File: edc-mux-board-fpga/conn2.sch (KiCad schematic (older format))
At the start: 24 parts

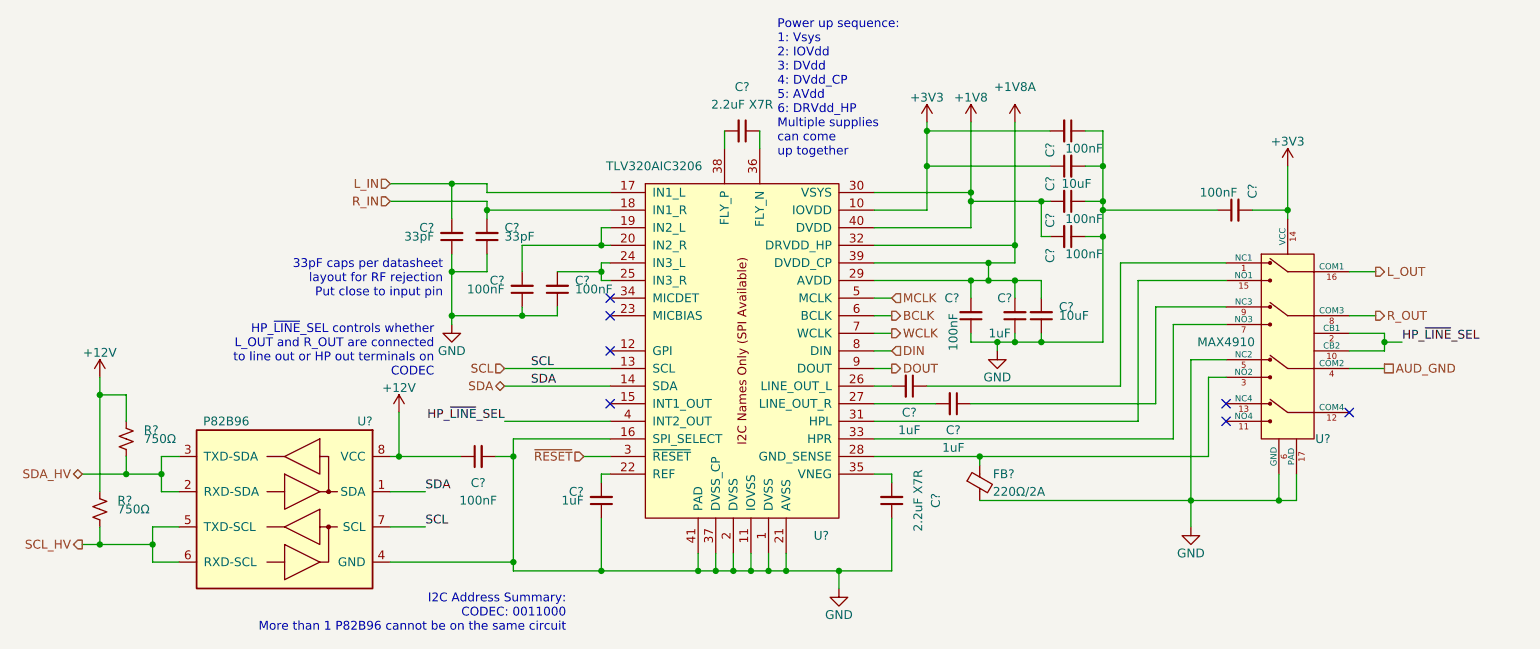
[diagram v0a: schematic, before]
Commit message: Finished FPGA and MCU interconnections.
Finished up interrupt wiring
Fixed a few missing connections
Annotated Schematic
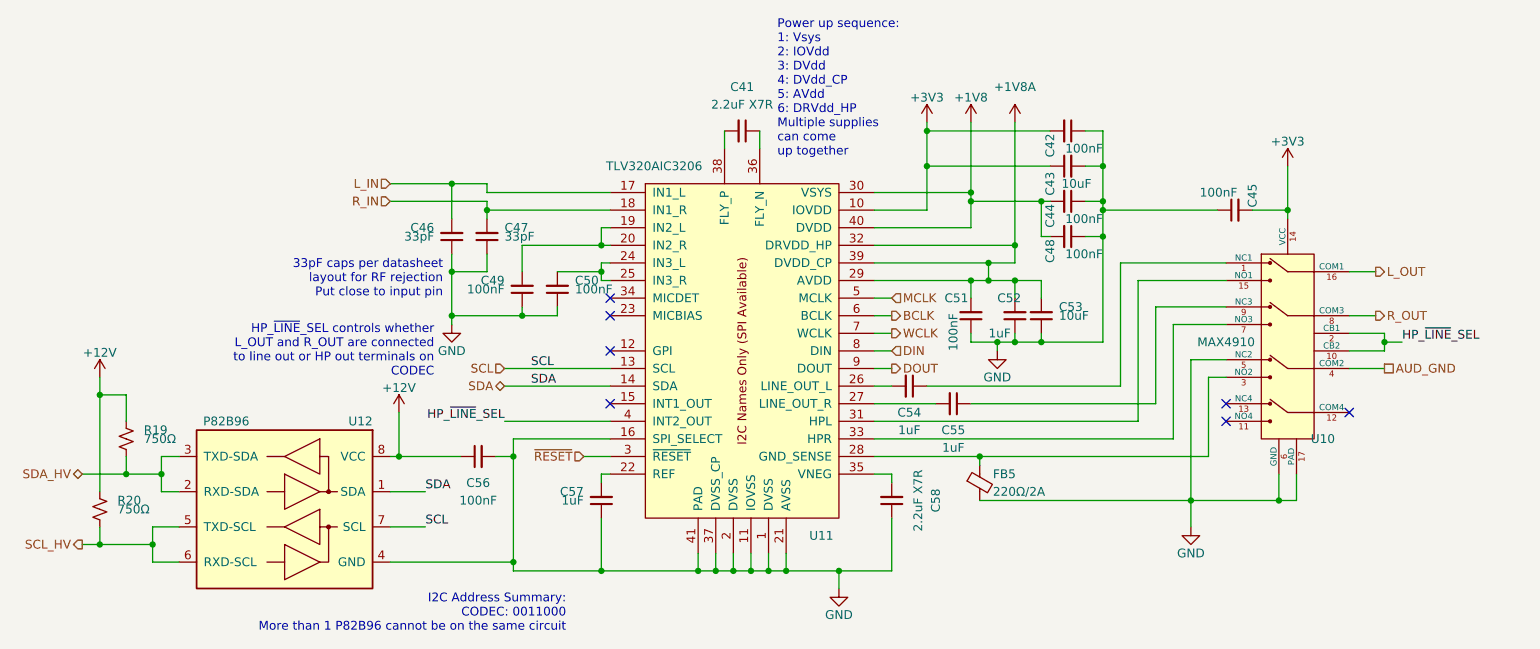
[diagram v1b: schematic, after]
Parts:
- removed C? (x2): 1uF, Capacitor_SMD:C_0805_2012Metric, symbol Device:C_Small
- removed C?: 2.2uF X7R, Capacitor_SMD:C_0603_1608Metric, symbol Device:C_Small
- removed C? (x2): 1uF, Capacitor_SMD:C_0603_1608Metric, symbol Device:C_Small
- removed C? (x8): 100nF, Capacitor_SMD:C_0603_1608Metric, symbol Device:C_Small
- removed C? (x2): 33pF, Capacitor_SMD:C_0603_1608Metric, symbol Device:C_Small
- removed C?: 10uF, Capacitor_SMD:C_1206_3216Metric, symbol Device:C_Small
- removed FB?: 220Ω/2A, Resistor_SMD:R_0603_1608Metric, symbol Device:Ferrite_Bead_Small
- removed R?: 750Ω, Resistor_SMD:R_0603_1608Metric, symbol Device:R_Small_US
- removed U?: TLV320AIC3206, Package_DFN_QFN:UQFN-40-1EP_5x5mm_P0.4mm_EP3.8x3.8mm_ThermalVias, symbol SW-Texas:TLV320AIC3206
- removed U?: MAX4910, Package_DFN_QFN:TQFN-16-1EP_3x3mm_P0.5mm_EP1.23x1.23mm, symbol SW-dallas-semi-maxim:MAX4910
- removed U?: P82B96, Package_SO:TSSOP-8_3x3mm_P0.65mm, symbol Interface_Expansion:P82B96
- added C42, C44, C45, C48, C49, C50, C51, C56: 100nF, Capacitor_SMD:C_0603_1608Metric, symbol Device:C_Small
- added C43: 10uF, Capacitor_SMD:C_1206_3216Metric, symbol Device:C_Small
- added C46, C47: 33pF, Capacitor_SMD:C_0603_1608Metric, symbol Device:C_Small
- added C52, C57: 1uF, Capacitor_SMD:C_0603_1608Metric, symbol Device:C_Small
- added C54, C55: 1uF, Capacitor_SMD:C_0805_2012Metric, symbol Device:C_Small
- added C58: 2.2uF X7R, Capacitor_SMD:C_0603_1608Metric, symbol Device:C_Small
- added FB5: 220Ω/2A, Resistor_SMD:R_0603_1608Metric, symbol Device:Ferrite_Bead_Small
- added R19: 750Ω, Resistor_SMD:R_0603_1608Metric, symbol Device:R_Small_US
- added U10: MAX4910, Package_DFN_QFN:TQFN-16-1EP_3x3mm_P0.5mm_EP1.23x1.23mm, symbol SW-dallas-semi-maxim:MAX4910
- added U11: TLV320AIC3206, Package_DFN_QFN:UQFN-40-1EP_5x5mm_P0.4mm_EP3.8x3.8mm_ThermalVias, symbol SW-Texas:TLV320AIC3206
- added U12: P82B96, Package_SO:TSSOP-8_3x3mm_P0.65mm, symbol Interface_Expansion:P82B96
- gave numbers to parts that had none: 3
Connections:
- net +12V: now also C56.1, R19.1, U12.8 (VCC)
- net +1V8: now also C44.2, C48.2, U11.30 (VSYS), U11.40 (DVDD)
- net +1V8A: now also C51.2, C52.2, U11.29 (AVDD), U11.32 (DRVDD_HP), U11.39 (DVDD_CP)
- net +3V3: now also C42.2, C43.1, C45.2, U10.14 (VCC), U11.10 (IOVDD)
- net AUD_GND: now also U10.4 (COM2)
- net BCLK: now also U11.6 (BCLK)
- net DIN: now also U11.8 (DIN)
- net DOUT: now also U11.9 (DOUT)
- net GND: now also C42.1, C43.2, C44.1, C45.1, C46.1, C47.1, C48.1, C49.1, C50.1, C51.1, C52.1, C56.2, C57.1, C58.1, FB5.2, U10.17 (PAD), U10.5 (NC2), U10.6 (GND), U11.1 (DVSS), U11.11 (IOVSS), U11.16 (SPI_SELECT), U11.2 (DVSS), U11.21 (AVSS), U11.37 (DVSS_CP), U11.41 (PAD), U12.4 (GND)
- net HP_~LINE~_SEL: now also U10.10 (CB2), U10.2 (CB1), U11.4 (INT2_OUT)
- net L_IN: now also C46.2, U11.17 (IN1_L)
- net L_OUT: now also U10.16 (COM1)
- net MCLK: now also U11.5 (MCLK)
- net R_IN: now also C47.2, U11.18 (IN1_R)
- net R_OUT: now also U10.8 (COM3)
- net SCL: now also U11.13 (SCL), U12.7 (SCL)
- net SCL_HV: now also U12.5 (TXD-SCL), U12.6 (RXD-SCL)
- net SDA: now also U11.14 (SDA), U12.1 (SDA)
- net SDA_HV: now also R19.2, U12.2 (RXD-SDA), U12.3 (TXD-SDA)
- net WCLK: now also U11.7 (WCLK)
- net ~RESET: now also U11.3 (~RESET)
- net at C41.1: now also U11.36 (FLY_N)
- net at C41.2: now also U11.38 (FLY_P)
- new net: C54.1, U10.1 (NC1)
- new net: C54.2, U11.26 (LINE_OUT_L)
- new net: C55.1, U10.9 (NC3)
- new net: C55.2, U11.27 (LINE_OUT_R)
- new net: C49.2, U11.19 (IN2_L), U11.20 (IN2_R)
- new net: C57.2, U11.22 (REF)
- new net: C50.2, U11.24 (IN3_L), U11.25 (IN3_R)
- new net: FB5.1, U10.3 (NO2), U11.28 (GND_SENSE)
- new net: U10.15 (NO1), U11.31 (HPL)
- new net: U10.7 (NO3), U11.33 (HPR)
- new net: C58.2, U11.35 (VNEG)
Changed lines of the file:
@@
 $EndDescr
 $Comp
-L SW-Texas:TLV320AIC3206 U?
-U 1 1 5CE6F2E7
+L SW-Texas:TLV320AIC3206 U11
+U 1 1 5DAC04B5
 P 5200 3400
-F 0 "U?" H 5650 2350 50  0000 C CNN
+F 0 "U11" H 5650 2350 50  0000 C CNN
 F 1 "TLV320AIC3206" H 4700 4450 50  0000 C CNN
 F 2 "Package_DFN_QFN:UQFN-40-1EP_5x5mm_P0.4mm_EP3.8x3.8mm_ThermalVias" H 5250 4800 50  0001 C CNN
@@
 $EndComp
 $Comp
-L Device:C_Small C?
+L Device:C_Small C41
 U 1 1 5CE6F309
 P 5200 2150
-F 0 "C?" V 4950 2150 50  0000 C CNN
+F 0 "C41" V 4950 2150 50  0000 C CNN
 F 1 "2.2uF X7R" V 5050 2150 50  0000 C CNN
 F 2 "Capacitor_SMD:C_0603_1608Metric" H 5200 2150 50  0001 C CNN
@@
 	5300 2250 5300 2150
 $Comp
-L Device:C_Small C?
-U 1 1 5CE6F311
+L Device:C_Small C58
+U 1 1 5DAC04CC
 P 6050 4250
-F 0 "C?" V 5800 4250 50  0000 C CNN
+F 0 "C58" V 5800 4250 50  0000 C CNN
 F 1 "2.2uF X7R" V 5900 4250 50  0000 C CNN
 F 2 "Capacitor_SMD:C_0603_1608Metric" H 6050 4250 50  0001 C CNN
@@
 	6050 4100 6050 4150
 $Comp
-L power:GND #PWR?
-U 1 1 5CE6F323
+L power:GND #PWR046
+U 1 1 5DAC04DB
 P 5750 4750
-F 0 "#PWR?" H 5750 4500 50  0001 C CNN
+F 0 "#PWR046" H 5750 4500 50  0001 C CNN
 F 1 "GND" H 5750 4600 50  0000 C CNN
 F 2 "" H 5750 4750 50  0001 C CNN
@@
 	5450 4650 5750 4650
 $Comp
-L Device:C_Small C?
-U 1 1 5CE6F329
+L Device:C_Small C57
+U 1 1 5DAC04F6
 P 4400 4250
-F 0 "C?" H 4500 4200 50  0000 L CNN
+F 0 "C57" H 4500 4200 50  0000 L CNN
 F 1 "1uF" H 4500 4250 50  0000 L CNN
 F 2 "Capacitor_SMD:C_0603_1608Metric" H 4400 4250 50  0001 C CNN
@@
 Connection ~ 4950 4650
 $Comp
-L Device:C_Small C?
-U 1 1 5CE6F348
+L Device:C_Small C49
+U 1 1 5DAC04FF
 P 3950 3050
-F 0 "C?" H 4050 3000 50  0000 L CNN
+F 0 "C49" H 4050 3000 50  0000 L CNN
 F 1 "100nF" H 4050 3050 50  0000 L CNN
 F 2 "Capacitor_SMD:C_0603_1608Metric" H 3950 3050 50  0001 C CNN
@@
 $EndComp
 $Comp
-L Device:C_Small C?
-U 1 1 5CE6F363
+L Device:C_Small C50
+U 1 1 5DAC050C
 P 4150 3050
-F 0 "C?" H 4050 3000 50  0000 R CNN
+F 0 "C50" H 4050 3000 50  0000 R CNN
 F 1 "100nF" H 4050 3050 50  0000 R CNN
 F 2 "Capacitor_SMD:C_0603_1608Metric" H 4150 3050 50  0001 C CNN
@@
 Connection ~ 4400 2950
 $Comp
-L power:GND #PWR?
-U 1 1 5CE6F368
+L power:GND #PWR041
+U 1 1 5DAC051C
 P 3550 3250
-F 0 "#PWR?" H 3550 3000 50  0001 C CNN
+F 0 "#PWR041" H 3550 3000 50  0001 C CNN
 F 1 "GND" H 3550 3100 50  0000 C CNN
 F 2 "" H 3550 3250 50  0001 C CNN
@@
 	8650 3300 8850 3300
 $Comp
-L SW-dallas-semi-maxim:MAX4910 U?
-U 1 1 5CE6F375
+L SW-dallas-semi-maxim:MAX4910 U10
+U 1 1 5DAC0526
 P 8300 3350
-F 0 "U?" H 8500 2800 50  0000 C CNN
+F 0 "U10" H 8500 2800 50  0000 C CNN
 F 1 "MAX4910" H 7950 3350 50  0000 C CNN
 F 2 "Package_DFN_QFN:TQFN-16-1EP_3x3mm_P0.5mm_EP1.23x1.23mm" H 9950 4500 50  0001 C CNN
@@
 	7750 3450 7750 4250
 $Comp
-L power:GND #PWR?
-U 1 1 5CE6F387
+L power:GND #PWR045
+U 1 1 5DAC0541
 P 7750 4400
-F 0 "#PWR?" H 7750 4150 50  0001 C CNN
+F 0 "#PWR045" H 7750 4150 50  0001 C CNN
 F 1 "GND" H 7750 4250 50  0000 C CNN
 F 2 "" H 7750 4400 50  0001 C CNN
@@
 	8650 3500 8850 3500
 $Comp
-L Device:Ferrite_Bead_Small FB?
-U 1 1 5CE6F39A
+L Device:Ferrite_Bead_Small FB5
+U 1 1 5DAC0551
 P 6550 4150
-F 0 "FB?" H 6625 4200 50  0000 L CNN
+F 0 "FB5" H 6625 4200 50  0000 L CNN
 F 1 "220Ω/2A" H 6625 4100 50  0000 L CNN
 F 2 "Resistor_SMD:R_0603_1608Metric" V 6480 4150 50  0001 C CNN
@@
 	3750 2600 4450 2600
 $Comp
-L Device:C_Small C?
-U 1 1 5CE6F3AC
+L Device:C_Small C46
+U 1 1 5DAC055E
 P 3550 2750
-F 0 "C?" H 3650 2700 50  0000 L CNN
+F 0 "C46" H 3650 2700 50  0000 L CNN
 F 1 "33pF" H 3650 2750 50  0000 L CNN
 F 2 "Capacitor_SMD:C_0603_1608Metric" H 3550 2750 50  0001 C CNN
@@
 	3200 2550 3750 2550
 $Comp
-L Device:C_Small C?
-U 1 1 5CE6F3B7
+L Device:C_Small C47
+U 1 1 5DAC056D
 P 3750 2750
-F 0 "C?" H 3650 2700 50  0000 R CNN
+F 0 "C47" H 3650 2700 50  0000 R CNN
 F 1 "33pF" H 3650 2750 50  0000 R CNN
 F 2 "Capacitor_SMD:C_0603_1608Metric" H 3750 2750 50  0001 C CNN
@@
 	5950 3000 6500 3000
 $Comp
-L SW-power:+1V8A #+1V8A?
-U 1 1 5CE6F3C8
+L SW-power:+1V8A #+1V8A04
+U 1 1 5DAC0576
 P 6750 2100
-F 0 "#+1V8A?" H 7500 1800 60  0001 C CNN
+F 0 "#+1V8A04" H 7500 1800 60  0001 C CNN
 F 1 "+1V8A" H 6750 2300 50  0000 C CNN
 F 2 "" H 6750 2100 60  0001 C CNN
@@
 $EndComp
 $Comp
-L power:+1V8 #PWR?
-U 1 1 5CE6F3D1
+L power:+1V8 #PWR039
+U 1 1 5DAC058D
 P 6500 2100
-F 0 "#PWR?" H 6500 1950 50  0001 C CNN
+F 0 "#PWR039" H 6500 1950 50  0001 C CNN
 F 1 "+1V8" H 6500 2240 50  0000 C CNN
 F 2 "" H 6500 2100 50  0001 C CNN
@@
 	6750 2800 6750 2900
 $Comp
-L power:+3V3 #PWR?
-U 1 1 5CE6F3E5
+L power:+3V3 #PWR038
+U 1 1 5DAC059C
 P 6250 2100
-F 0 "#PWR?" H 6250 1950 50  0001 C CNN
+F 0 "#PWR038" H 6250 1950 50  0001 C CNN
 F 1 "+3V3" H 6250 2240 50  0000 C CNN
 F 2 "" H 6250 2100 50  0001 C CNN
@@
 	6250 2600 6250 2350
 $Comp
-L Device:C_Small C?
-U 1 1 5CE6F3F4
+L Device:C_Small C52
+U 1 1 5DAC05A3
 P 6750 3200
-F 0 "C?" H 6850 3100 50  0000 R CNN
+F 0 "C52" H 6850 3100 50  0000 R CNN
 F 1 "1uF" H 6900 3300 50  0000 R CNN
 F 2 "Capacitor_SMD:C_0603_1608Metric" H 6750 3200 50  0001 C CNN
@@
 $EndComp
 $Comp
-L power:GND #PWR?
-U 1 1 5CE6F403
+L power:GND #PWR042
+U 1 1 5DAC05B5
 P 6650 3400
-F 0 "#PWR?" H 6650 3150 50  0001 C CNN
+F 0 "#PWR042" H 6650 3150 50  0001 C CNN
 F 1 "GND" H 6650 3250 50  0000 C CNN
 F 2 "" H 6650 3400 50  0001 C CNN
@@
 $EndComp
 $Comp
-L Device:C_Small C?
+L Device:C_Small C53
 U 1 1 5CE6F40F
 P 6900 3200
-F 0 "C?" H 6800 3150 50  0000 R CNN
+F 0 "C53" H 6800 3150 50  0000 R CNN
 F 1 "10uF" H 6800 3200 50  0000 R CNN
 F 2 "Capacitor_SMD:C_1206_3216Metric" H 6900 3200 50  0001 C CNN
@@
 $EndComp
 $Comp
-L Device:C_Small C?
-U 1 1 5CE6F425
+L Device:C_Small C51
+U 1 1 5DAC05CC
 P 6500 3200
-F 0 "C?" H 6650 3100 50  0000 R CNN
+F 0 "C51" H 6650 3100 50  0000 R CNN
 F 1 "100nF" V 6600 3400 50  0000 R CNN
 F 2 "Capacitor_SMD:C_0603_1608Metric" H 6500 3200 50  0001 C CNN
@@
 	6650 3350 6750 3350
 $Comp
-L Device:C_Small C?
-U 1 1 5CE6F42F
+L Device:C_Small C42
+U 1 1 5DAC05E4
 P 7050 2150
-F 0 "C?" H 7200 2050 50  0000 R CNN
+F 0 "C42" H 7200 2050 50  0000 R CNN
 F 1 "100nF" V 7150 2350 50  0000 R CNN
 F 2 "Capacitor_SMD:C_0603_1608Metric" H 7050 2150 50  0001 C CNN
@@
 $EndComp
 $Comp
-L Device:C_Small C?
-U 1 1 5CE6F439
+L Device:C_Small C43
+U 1 1 5DAC05EE
 P 7050 2350
-F 0 "C?" H 6950 2450 50  0000 C CNN
+F 0 "C43" H 6950 2450 50  0000 C CNN
 F 1 "10uF" V 6950 2300 50  0000 C CNN
 F 2 "Capacitor_SMD:C_1206_3216Metric" H 7050 2350 50  0001 C CNN
@@
 	6250 2150 6250 2100
 $Comp
-L Device:C_Small C?
-U 1 1 5CE6F451
+L Device:C_Small C44
+U 1 1 5DAC0601
 P 7050 2550
-F 0 "C?" H 7200 2450 50  0000 R CNN
+F 0 "C44" H 7200 2450 50  0000 R CNN
 F 1 "100nF" V 7150 2750 50  0000 R CNN
 F 2 "Capacitor_SMD:C_0603_1608Metric" H 7050 2550 50  0001 C CNN
@@
 	6500 2550 6500 2500
 $Comp
-L Device:C_Small C?
-U 1 1 5CE6F456
+L Device:C_Small C48
+U 1 1 5DAC0606
 P 7050 2750
-F 0 "C?" H 7200 2650 50  0000 R CNN
+F 0 "C48" H 7200 2650 50  0000 R CNN
 F 1 "100nF" V 7150 2950 50  0000 R CNN
 F 2 "Capacitor_SMD:C_0603_1608Metric" H 7050 2750 50  0001 C CNN
@@
 NoConn ~ 8650 3750
 $Comp
-L Device:C_Small C?
-U 1 1 5CE6F46F
+L Device:C_Small C45
+U 1 1 5DAC061C
 P 8000 2600
-F 0 "C?" H 8150 2500 50  0000 R CNN
+F 0 "C45" H 8150 2500 50  0000 R CNN
 F 1 "100nF" V 8100 2800 50  0000 R CNN
 F 2 "Capacitor_SMD:C_0603_1608Metric" H 8000 2600 50  0001 C CNN
@@
 $EndComp
 $Comp
-L power:+3V3 #PWR?
-U 1 1 5CE6F47E
+L power:+3V3 #PWR040
+U 1 1 5DAC0631
 P 8300 2350
-F 0 "#PWR?" H 8300 2200 50  0001 C CNN
+F 0 "#PWR040" H 8300 2200 50  0001 C CNN
 F 1 "+3V3" H 8300 2490 50  0000 C CNN
 F 2 "" H 8300 2350 50  0001 C CNN
@@
 	8250 4250 8350 4250
 $Comp
-L Interface_Expansion:P82B96 U?
-U 1 1 5CE6F489
+L Interface_Expansion:P82B96 U12
+U 1 1 5DAC0639
 P 2600 4300
-F 0 "U?" H 2100 4800 50  0000 L CNN
+F 0 "U12" H 2100 4800 50  0000 L CNN
 F 1 "P82B96" H 2800 4800 50  0000 L CNN
 F 2 "Package_SO:TSSOP-8_3x3mm_P0.65mm" H 2600 4300 50  0001 C CNN
@@
 $EndComp
 $Comp
-L power:+12V #PWR?
-U 1 1 5CE6F490
+L power:+12V #PWR043
+U 1 1 5DAC0650
 P 1550 3550
-F 0 "#PWR?" H 1550 3400 50  0001 C CNN
+F 0 "#PWR043" H 1550 3400 50  0001 C CNN
 F 1 "+12V" H 1550 3690 50  0000 C CNN
 F 2 "" H 1550 3550 50  0001 C CNN
@@
 	1900 4100 1900 4200
 $Comp
-L Device:R_Small_US R?
-U 1 1 5CE6F4C1
+L Device:R_Small_US R19
+U 1 1 5DAC0654
 P 1700 3900
-F 0 "R?" H 1800 3950 50  0000 L CNN
+F 0 "R19" H 1800 3950 50  0000 L CNN
 F 1 "750Ω" H 1800 3900 50  0000 L CNN
 F 2 "Resistor_SMD:R_0603_1608Metric" H 1700 3900 50  0001 C CNN
@@
 $EndComp
 $Comp
-L Device:R_Small_US R?
+L Device:R_Small_US R20
 U 1 1 5CE6F4D0
 P 1550 4300
-F 0 "R?" H 1650 4350 50  0000 L CNN
+F 0 "R20" H 1650 4350 50  0000 L CNN
 F 1 "750Ω" H 1650 4300 50  0000 L CNN
 F 2 "Resistor_SMD:R_0603_1608Metric" H 1550 4300 50  0001 C CNN
@@
 	1700 4100 1900 4100
 $Comp
-L power:+12V #PWR?
-U 1 1 5CE6F4E1
+L power:+12V #PWR044
+U 1 1 5DAC0678
 P 3250 3750
-F 0 "#PWR?" H 3250 3600 50  0001 C CNN
+F 0 "#PWR044" H 3250 3600 50  0001 C CNN
 F 1 "+12V" H 3250 3890 50  0000 C CNN
 F 2 "" H 3250 3750 50  0001 C CNN
@@
 	3200 4400 3400 4400
 $Comp
-L Device:C_Small C?
-U 1 1 5CE6F4F3
+L Device:C_Small C56
+U 1 1 5DAC0685
 P 3700 4000
-F 0 "C?" V 3550 4000 50  0000 C CNN
+F 0 "C56" V 3550 4000 50  0000 C CNN
 F 1 "100nF" V 3450 4000 50  0000 C CNN
 F 2 "Capacitor_SMD:C_0603_1608Metric" H 3700 4000 50  0001 C CNN
@@
 	1450 4500 1550 4500
 $Comp
-L Device:C_Small C?
-U 1 1 5CE6F2C0
+L Device:C_Small C54
+U 1 1 5DAC048F
 P 6150 3600
-F 0 "C?" V 6300 3600 50  0000 C CNN
+F 0 "C54" V 6300 3600 50  0000 C CNN
 F 1 "1uF" V 6400 3600 50  0000 C CNN
 F 2 "Capacitor_SMD:C_0805_2012Metric" H 6150 3600 50  0001 C CNN
@@
 $EndComp
 $Comp
-L Device:C_Small C?
-U 1 1 5CE6F2D4
+L Device:C_Small C55
+U 1 1 5DAC04A0
 P 6400 3700
-F 0 "C?" V 6550 3700 50  0000 C CNN
+F 0 "C55" V 6550 3700 50  0000 C CNN
 F 1 "1uF" V 6650 3700 50  0000 C CNN
 F 2 "Capacitor_SMD:C_0805_2012Metric" H 6400 3700 50  0001 C CNN

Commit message: assigned more footprints
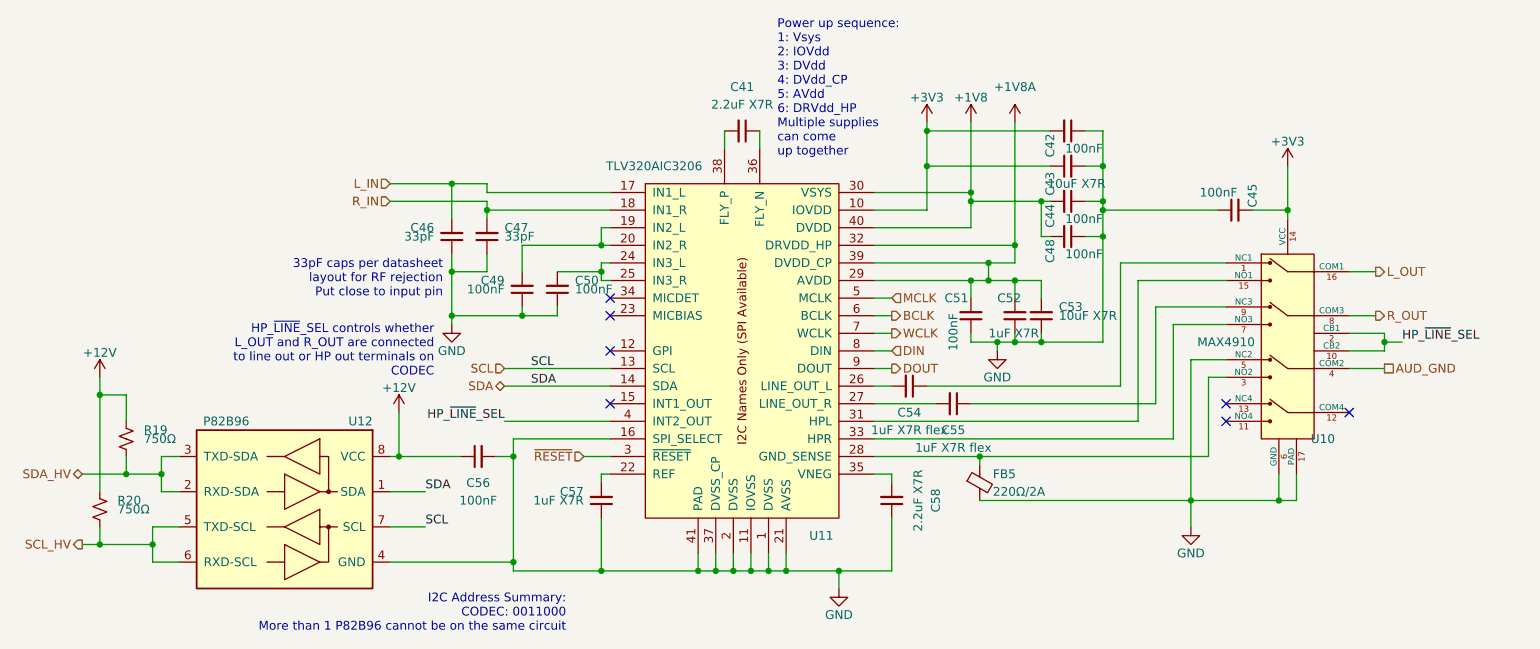
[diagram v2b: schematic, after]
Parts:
- C43, C53: value 10uF -> 10uF X7R
- C52, C57: value 1uF -> 1uF X7R
- C54, C55: value 1uF -> 1uF X7R flex
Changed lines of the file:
@@
 P 4400 4250
 F 0 "C57" H 4500 4200 50  0000 L CNN
-F 1 "1uF" H 4500 4250 50  0000 L CNN
+F 1 "1uF X7R" H 4500 4250 50  0000 L CNN
 F 2 "Capacitor_SMD:C_0603_1608Metric" H 4400 4250 50  0001 C CNN
 F 3 "~" H 4400 4250 50  0001 C CNN
@@
 P 6750 3200
 F 0 "C52" H 6850 3100 50  0000 R CNN
-F 1 "1uF" H 6900 3300 50  0000 R CNN
+F 1 "1uF X7R" H 6900 3300 50  0000 R CNN
 F 2 "Capacitor_SMD:C_0603_1608Metric" H 6750 3200 50  0001 C CNN
 F 3 "~" H 6750 3200 50  0001 C CNN
@@
 P 6900 3200
 F 0 "C53" H 6800 3150 50  0000 R CNN
-F 1 "10uF" H 6800 3200 50  0000 R CNN
+F 1 "10uF X7R" H 6800 3200 50  0000 R CNN
 F 2 "Capacitor_SMD:C_1206_3216Metric" H 6900 3200 50  0001 C CNN
 F 3 "~" H 6900 3200 50  0001 C CNN
@@
 P 7050 2350
 F 0 "C43" H 6950 2450 50  0000 C CNN
-F 1 "10uF" V 6950 2300 50  0000 C CNN
+F 1 "10uF X7R" V 6950 2300 50  0000 C CNN
 F 2 "Capacitor_SMD:C_1206_3216Metric" H 7050 2350 50  0001 C CNN
 F 3 "~" H 7050 2350 50  0001 C CNN
@@
 P 6150 3600
 F 0 "C54" V 6300 3600 50  0000 C CNN
-F 1 "1uF" V 6400 3600 50  0000 C CNN
+F 1 "1uF X7R flex" V 6400 3600 50  0000 C CNN
 F 2 "Capacitor_SMD:C_0805_2012Metric" H 6150 3600 50  0001 C CNN
 F 3 "~" H 6150 3600 50  0001 C CNN
@@
 P 6400 3700
 F 0 "C55" V 6550 3700 50  0000 C CNN
-F 1 "1uF" V 6650 3700 50  0000 C CNN
+F 1 "1uF X7R flex" V 6650 3700 50  0000 C CNN
 F 2 "Capacitor_SMD:C_0805_2012Metric" H 6400 3700 50  0001 C CNN
 F 3 "~" H 6400 3700 50  0001 C CNN
